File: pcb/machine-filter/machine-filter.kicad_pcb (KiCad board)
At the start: 2 copper layers, 150 x 107 mm, 162 parts, among them J1 PJ398SM, J10 PJ398SM, J11 PJ398SM, J12 PJ398SM, J13 EURO PWR 2x5, J14 EXPANSION 2x4, J15 TF-01A, J2 PJ398SM, J3 PJ398SM, J4 PJ398SM, J5 PJ398SM, J6 PJ398SM, J7 PJ398SM, J8 PJ398SM, J9 PJ398SM, U1 LMV324, U2 LMV324, U3 TL072, U4 TL072, U5 LM4040-10, U6 74HC4051, U7 LM324, U8 LM324

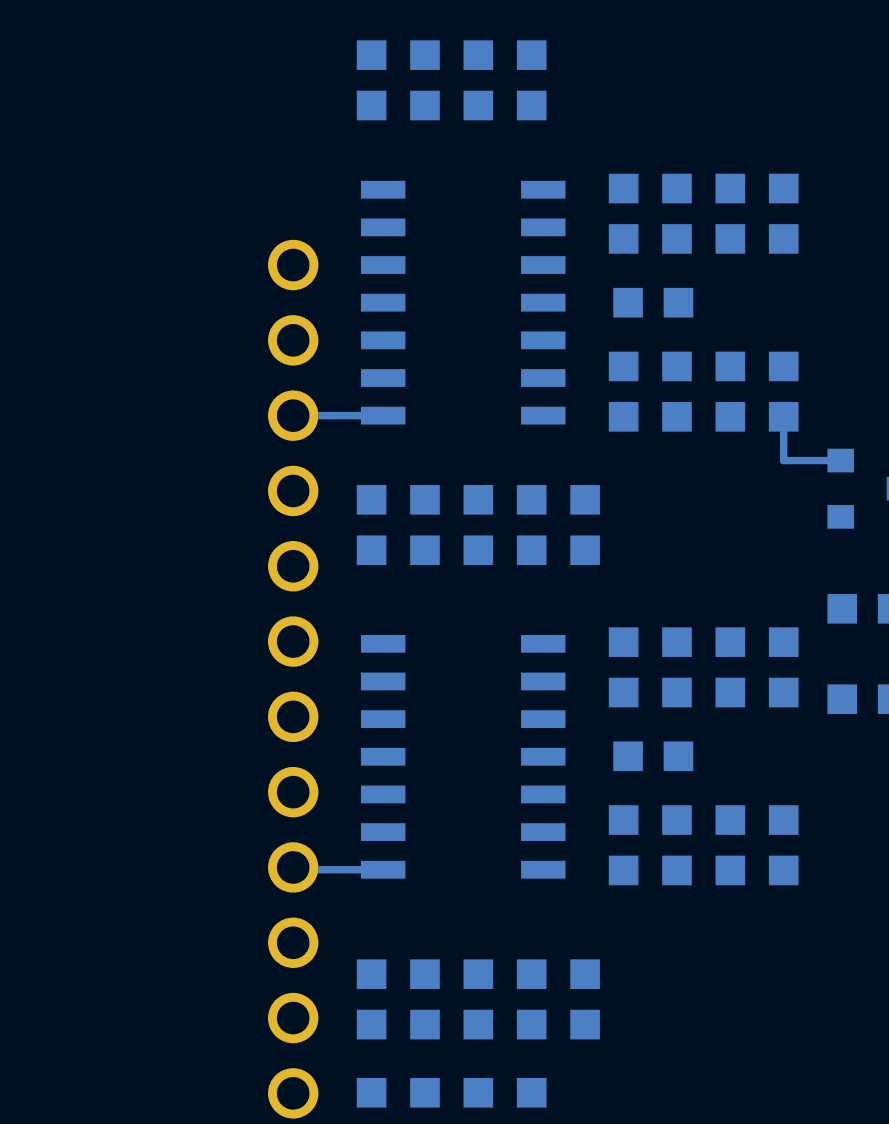
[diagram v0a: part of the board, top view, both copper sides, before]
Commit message: Traces: all eight CV op-amp outputs -> Seed3 ADC pins (d)
Four on the back, four through a via to the front; DRC clean except the
R70/R100 courtyard overlap.

Co-Authored-By: Claude Opus 5.5 <noreply@anthropic.com>
Claude-Session: https://claude.ai/code/session_01Cf5qNBi3oNHhbCjPHvswth
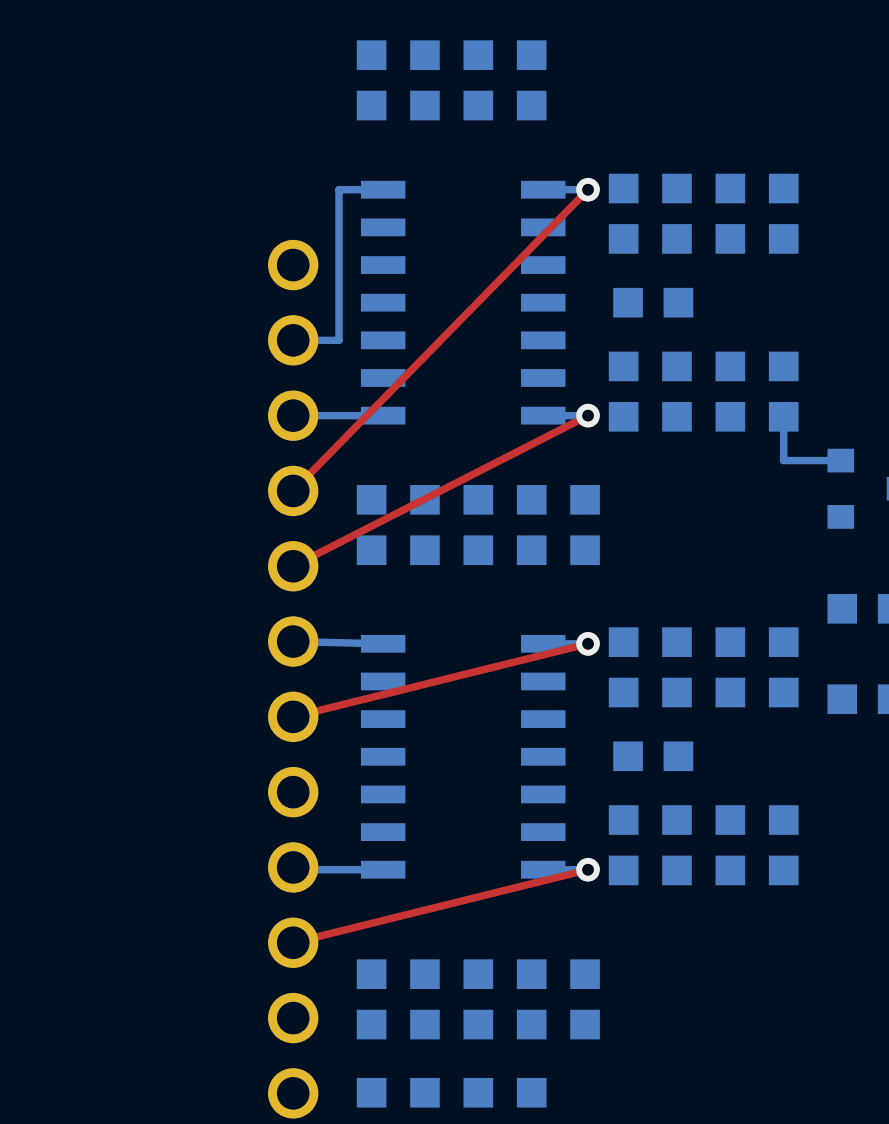
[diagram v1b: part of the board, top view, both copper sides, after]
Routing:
- net ADC_LPRES: track 0.00 -> 15.7 mm, vias 0 -> 1
- net ADC_EQF: track 0.00 -> 12.7 mm, vias 0 -> 1
- net ADC_SRR: track 0.00 -> 11.8 mm, vias 0 -> 1
- net ADC_DIST: track 0.00 -> 11.8 mm, vias 0 -> 1
- net ADC_HPRES: track 0.00 -> 8.11 mm
- net ADC_EQG: track 0.00 -> 3.04 mm
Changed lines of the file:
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@@
 		(net "ADC_BASE")
+	)
+	(segment
+		(start 238.8 88.69)
+		(end 228.855 98.85)
+		(width 0.25)
+		(layer "F.Cu")
+		(net "ADC_LPRES")
+	)
+	(via
+		(at 238.8 88.69)
+		(size 0.8)
+		(drill 0.4)
+		(layers "F.Cu" "B.Cu")
+		(net "ADC_LPRES")
+	)
+	(segment
+		(start 237.29 88.69)
+		(end 238.8 88.69)
+		(width 0.25)
+		(layer "B.Cu")
+		(net "ADC_LPRES")
+	)
+	(segment
+		(start 231.89 88.69)
+		(end 230.4 88.69)
+		(width 0.25)
+		(layer "B.Cu")
+		(net "ADC_HPRES")
+	)
+	(segment
+		(start 230.4 88.69)
+		(end 230.4 93.77)
+		(width 0.25)
+		(layer "B.Cu")
+		(net "ADC_HPRES")
+	)
+	(segment
+		(start 230.4 93.77)
+		(end 228.855 93.77)
+		(width 0.25)
+		(layer "B.Cu")
+		(net "ADC_HPRES")
+	)
+	(segment
+		(start 238.8 96.31)
+		(end 228.855 101.39)
+		(width 0.25)
+		(layer "F.Cu")
+		(net "ADC_EQF")
+	)
+	(via
+		(at 238.8 96.31)
+		(size 0.8)
+		(drill 0.4)
+		(layers "F.Cu" "B.Cu")
+		(net "ADC_EQF")
+	)
+	(segment
+		(start 237.29 96.31)
+		(end 238.8 96.31)
+		(width 0.25)
+		(layer "B.Cu")
+		(net "ADC_EQF")
+	)
+	(segment
+		(start 231.89 104.007)
+		(end 228.855 103.93)
+		(width 0.25)
+		(layer "B.Cu")
+		(net "ADC_EQG")
+	)
+	(segment
+		(start 238.8 104.007)
+		(end 228.855 106.47)
+		(width 0.25)
+		(layer "F.Cu")
+		(net "ADC_DIST")
+	)
+	(via
+		(at 238.8 104.007)
+		(size 0.8)
+		(drill 0.4)
+		(layers "F.Cu" "B.Cu")
+		(net "ADC_DIST")
+	)
+	(segment
+		(start 237.29 104.007)
+		(end 238.8 104.007)
+		(width 0.25)
+		(layer "B.Cu")
+		(net "ADC_DIST")
+	)
+	(segment
+		(start 238.8 111.627)
+		(end 228.855 114.09)
+		(width 0.25)
+		(layer "F.Cu")
+		(net "ADC_SRR")
+	)
+	(via
+		(at 238.8 111.627)
+		(size 0.8)
+		(drill 0.4)
+		(layers "F.Cu" "B.Cu")
+		(net "ADC_SRR")
+	)
+	(segment
+		(start 237.29 111.627)
+		(end 238.8 111.627)
+		(width 0.25)
+		(layer "B.Cu")
+		(net "ADC_SRR")
 	)
 	(embedded_fonts no)

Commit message: Control board panel parts placed at their fixed positions (d)
Co-Authored-By: Claude Opus 5.5 <noreply@anthropic.com>
Claude-Session: https://claude.ai/code/session_01Cf5qNBi3oNHhbCjPHvswth
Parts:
- moved J10 206.0 mm to (163.2, 141.3), turned to 90 degrees
- moved D5 203.1 mm to (160.7, 114.9), turned to 90 degrees
- moved J6 201.7 mm to (163.2, 102.2), turned to 90 degrees
- moved D7 193.6 mm to (160.7, 134.5), turned to 90 degrees
- moved J2 191.9 mm to (163.2, 82.8)
- moved J1 190.5 mm to (150.7, 82.8)
- moved D6 187.0 mm to (148.2, 134.5), turned to 90 degrees
- moved D9 186.4 mm to (160.7, 154.0), turned to 90 degrees
- moved J11 185.3 mm to (150.7, 160.8), turned to 90 degrees
- moved J12 183.1 mm to (163.2, 160.8), turned to 90 degrees
- moved D8 180.0 mm to (148.2, 154.0), turned to 90 degrees
- moved J7 177.4 mm to (150.7, 121.7), turned to 90 degrees
- moved J8 175.0 mm to (163.2, 121.7), turned to 90 degrees
- moved RV9 172.4 mm to (132.9, 160.5), turned to 180 degrees
- moved J4 169.5 mm to (163.2, 69.8), turned to 180 degrees
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
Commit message: Straighten traces (d): horizontal/vertical segments only; no diagonals left
Co-Authored-By: Claude Opus 5.5 <noreply@anthropic.com>
Claude-Session: https://claude.ai/code/session_01Cf5qNBi3oNHhbCjPHvswth
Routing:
- net ADC_LPRES: track 15.7 -> 21.6 mm
- net ADC_EQF: track 12.7 -> 16.5 mm
- net ADC_SRR: track 11.8 -> 13.9 mm
- net ADC_DIST: track 11.8 -> 13.9 mm
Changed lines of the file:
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@@
-	)
-	(segment
-		(start 228.855 111.627)
-		(end 228.855 111.55)
-		(width 0.25)
-		(layer "B.Cu")
-		(net "ADC_WIDTH")
 	)
 	(segment
@@
 	)
 	(segment
+		(start 231.2 88.69)
+		(end 231.2 98.85)
+		(width 0.25)
+		(layer "F.Cu")
+		(net "ADC_LPRES")
+	)
+	(segment
 		(start 238.8 88.69)
+		(end 231.2 88.69)
+		(width 0.25)
+		(layer "F.Cu")
+		(net "ADC_LPRES")
+	)
+	(segment
+		(start 231.2 98.85)
 		(end 228.855 98.85)
 		(width 0.25)
@@
 	)
 	(segment
+		(start 232.4 96.31)
+		(end 232.4 101.39)
+		(width 0.25)
+		(layer "F.Cu")
+		(net "ADC_EQF")
+	)
+	(segment
+		(start 232.4 101.39)
+		(end 228.855 101.39)
+		(width 0.25)
+		(layer "F.Cu")
+		(net "ADC_EQF")
+	)
+	(segment
 		(start 238.8 96.31)
-		(end 228.855 101.39)
+		(end 232.4 96.31)
 		(width 0.25)
 		(layer "F.Cu")
@@
 	(segment
 		(start 231.89 104.007)
-		(end 228.855 103.93)
+		(end 228.855 104.007)
 		(width 0.25)
 		(layer "B.Cu")
@@
 	)
 	(segment
+		(start 231.2 106.47)
+		(end 228.855 106.47)
+		(width 0.25)
+		(layer "F.Cu")
+		(net "ADC_DIST")
+	)
+	(segment
 		(start 238.8 104.007)
-		(end 228.855 106.47)
+		(end 231.2 104.007)
+		(width 0.25)
+		(layer "F.Cu")
+		(net "ADC_DIST")
+	)
+	(segment
+		(start 231.2 104.007)
+		(end 231.2 106.47)
 		(width 0.25)
 		(layer "F.Cu")
@@
 	)
 	(segment
+		(start 231.2 111.627)
+		(end 231.2 114.09)
+		(width 0.25)
+		(layer "F.Cu")
+		(net "ADC_SRR")
+	)
+	(segment
 		(start 238.8 111.627)
+		(end 231.2 111.627)
+		(width 0.25)
+		(layer "F.Cu")
+		(net "ADC_SRR")
+	)
+	(segment
+		(start 231.2 114.09)
 		(end 228.855 114.09)
 		(width 0.25)

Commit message: Reroute far-side ADC traces to the layer convention (back vertical, front horizontal); C21 nudged; sorted DRC tool
Co-Authored-By: Claude Opus 5.5 <noreply@anthropic.com>
Claude-Session: https://claude.ai/code/session_01Cf5qNBi3oNHhbCjPHvswth
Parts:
- moved C21 0.60 mm to (241.6, 92.5)
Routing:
- net ADC_LPRES: track 21.6 -> 23.2 mm, vias 1 -> 2
- net ADC_SRR: vias 1 -> 2
- net ADC_EQF: vias 1 -> 2
- net ADC_DIST: vias 1 -> 2
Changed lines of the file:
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@@
 	(footprint "filter-module:C_0603"
 		(layer "B.Cu")
-		(at 241 92.5)
+		(at 241.6 92.5)
 		(descr "Capacitor SMD 0603, reflow soldering, AVX (see smccp.pdf)")
 		(tags "capacitor 0603 C0603")
@@
 	)
 	(segment
-		(start 231.2 88.69)
-		(end 231.2 98.85)
-		(width 0.25)
-		(layer "F.Cu")
-		(net "ADC_LPRES")
-	)
-	(segment
-		(start 238.8 88.69)
-		(end 231.2 88.69)
-		(width 0.25)
-		(layer "F.Cu")
-		(net "ADC_LPRES")
-	)
-	(segment
-		(start 231.2 98.85)
+		(start 239.6 98.85)
 		(end 228.855 98.85)
 		(width 0.25)
@@
 		(net "ADC_LPRES")
 	)
+	(via
+		(at 239.6 98.85)
+		(size 0.8)
+		(drill 0.4)
+		(layers "F.Cu" "B.Cu")
+		(net "ADC_LPRES")
+	)
+	(segment
+		(start 239.6 88.69)
+		(end 239.6 98.85)
+		(width 0.25)
+		(layer "B.Cu")
+		(net "ADC_LPRES")
+	)
+	(segment
+		(start 238.8 88.69)
+		(end 239.6 88.69)
+		(width 0.25)
+		(layer "B.Cu")
+		(net "ADC_LPRES")
+	)
 	(segment
 		(start 237.29 88.69)
@@
 	)
 	(segment
-		(start 232.4 96.31)
-		(end 232.4 101.39)
-		(width 0.25)
-		(layer "F.Cu")
-		(net "ADC_EQF")
-	)
-	(segment
-		(start 232.4 101.39)
+		(start 238.8 101.39)
 		(end 228.855 101.39)
 		(width 0.25)
@@
 		(net "ADC_EQF")
 	)
-	(segment
-		(start 238.8 96.31)
-		(end 232.4 96.31)
-		(width 0.25)
-		(layer "F.Cu")
+	(via
+		(at 238.8 101.39)
+		(size 0.8)
+		(drill 0.4)
+		(layers "F.Cu" "B.Cu")
 		(net "ADC_EQF")
 	)
@@
 	)
 	(segment
+		(start 238.8 96.31)
+		(end 238.8 101.39)
+		(width 0.25)
+		(layer "B.Cu")
+		(net "ADC_EQF")
+	)
+	(segment
 		(start 231.89 104.007)
 		(end 228.855 104.007)
@@
 	)
 	(segment
-		(start 231.2 106.47)
+		(start 238.8 106.47)
 		(end 228.855 106.47)
 		(width 0.25)
@@
 		(net "ADC_DIST")
 	)
-	(segment
-		(start 238.8 104.007)
-		(end 231.2 104.007)
-		(width 0.25)
-		(layer "F.Cu")
-		(net "ADC_DIST")
-	)
-	(segment
-		(start 231.2 104.007)
-		(end 231.2 106.47)
-		(width 0.25)
-		(layer "F.Cu")
+	(via
+		(at 238.8 106.47)
+		(size 0.8)
+		(drill 0.4)
+		(layers "F.Cu" "B.Cu")
 		(net "ADC_DIST")
 	)
@@
 	)
 	(segment
-		(start 231.2 111.627)
-		(end 231.2 114.09)
+		(start 238.8 104.007)
+		(end 238.8 106.47)
 		(width 0.25)
-		(layer "F.Cu")
-		(net "ADC_SRR")
+		(layer "B.Cu")
+		(net "ADC_DIST")
 	)
 	(segment
-		(start 238.8 111.627)
-		(end 231.2 111.627)
+		(start 238.8 114.09)
+		(end 228.855 114.09)
 		(width 0.25)
 		(layer "F.Cu")
 		(net "ADC_SRR")
 	)
-	(segment
-		(start 231.2 114.09)
-		(end 228.855 114.09)
-		(width 0.25)
-		(layer "F.Cu")
+	(via
+		(at 238.8 114.09)
+		(size 0.8)
+		(drill 0.4)
+		(layers "F.Cu" "B.Cu")
 		(net "ADC_SRR")
 	)
@@
 		(net "ADC_SRR")
 	)
+	(segment
+		(start 238.8 111.627)
+		(end 238.8 114.09)
+		(width 0.25)
+		(layer "B.Cu")
+		(net "ADC_SRR")
+	)

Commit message: J14 placed sideways by the USB pins; USB D-/D+ traces round the header (d)
Co-Authored-By: Claude Opus 5.5 <noreply@anthropic.com>
Claude-Session: https://claude.ai/code/session_01Cf5qNBi3oNHhbCjPHvswth
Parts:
- moved J14 2.49 mm to (236.5, 130.6)
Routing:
- net /Main: Daisy Seed3/USB_DM: track 0.00 -> 14.0 mm
- net /Main: Daisy Seed3/USB_DP: track 0.00 -> 11.5 mm
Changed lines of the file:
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@@
 	(footprint "filter-module:Pins_2x04_2.54mm_TH"
 		(layer "B.Cu")
-		(at 238.155 128.735 90)
+		(at 236.5 130.6 90)
 		(descr "Through hole straight socket strip, 2x04, 2.54mm pitch, double rows")
 		(tags "Through hole socket strip THT 2x04 2.54mm double row")
@@
 		(net "ADC_SRR")
 	)
+	(segment
+		(start 230.6 128.06)
+		(end 240.31 128.06)
+		(width 0.25)
+		(layer "B.Cu")
+		(net "/Main: Daisy Seed3/USB_DM")
+	)
+	(segment
+		(start 230.6 129.33)
+		(end 230.6 128.06)
+		(width 0.25)
+		(layer "B.Cu")
+		(net "/Main: Daisy Seed3/USB_DM")
+	)
+	(segment
+		(start 240.31 128.06)
+		(end 240.31 129.33)
+		(width 0.25)
+		(layer "B.Cu")
+		(net "/Main: Daisy Seed3/USB_DM")
+	)
+	(segment
+		(start 228.855 129.33)
+		(end 230.6 129.33)
+		(width 0.25)
+		(layer "B.Cu")
+		(net "/Main: Daisy Seed3/USB_DM")
+	)
+	(segment
+		(start 231.2 133.139999)
+		(end 237.77 133.139999)
+		(width 0.25)
+		(layer "B.Cu")
+		(net "/Main: Daisy Seed3/USB_DP")
+	)
+	(segment
+		(start 228.855 131.87)
+		(end 231.2 131.87)
+		(width 0.25)
+		(layer "B.Cu")
+		(net "/Main: Daisy Seed3/USB_DP")
+	)
+	(segment
+		(start 237.77 133.139999)
+		(end 237.77 131.87)
+		(width 0.25)
+		(layer "B.Cu")
+		(net "/Main: Daisy Seed3/USB_DP")
+	)
+	(segment
+		(start 231.2 131.87)
+		(end 231.2 133.139999)
+		(width 0.25)
+		(layer "B.Cu")
+		(net "/Main: Daisy Seed3/USB_DP")
+	)
 	(embedded_fonts no)
